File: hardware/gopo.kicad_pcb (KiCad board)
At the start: 4 copper layers, 65.9 x 40.6 mm, 139 parts, among them J3 TFT032B018, J4 SolderWire-1.5sqmm, J7 USB_C_Receptacle_USB2.0_16P, J8 2-CH UART TO ETH, Q1 BSS138P, Q2 BSS138P, Q3 SQJB60EP, Q4 BSS138P, Q5 SQJB60EP, Q6 BSS138P, Q7 IRLML6344, Q8 TSM3443CX6, SW1 BOOT / PTS810, SW2 RESET / PTS810, SW3 L-KLS4-EC1121S-E5A-F12.5, U1 AP33772SDKZ-13-FA02, U10 USBLC6-2SC6, U11 TPS55340PWPR, U12 LM74801-Q1, U13 74LVC1G08, U2 ESP32-C6-MINI-1-H4, U3 INA226, U4 BQ32000, U5 AOZ1284PI, U6 TLV431BQDBZT, Y1 32.768kHz

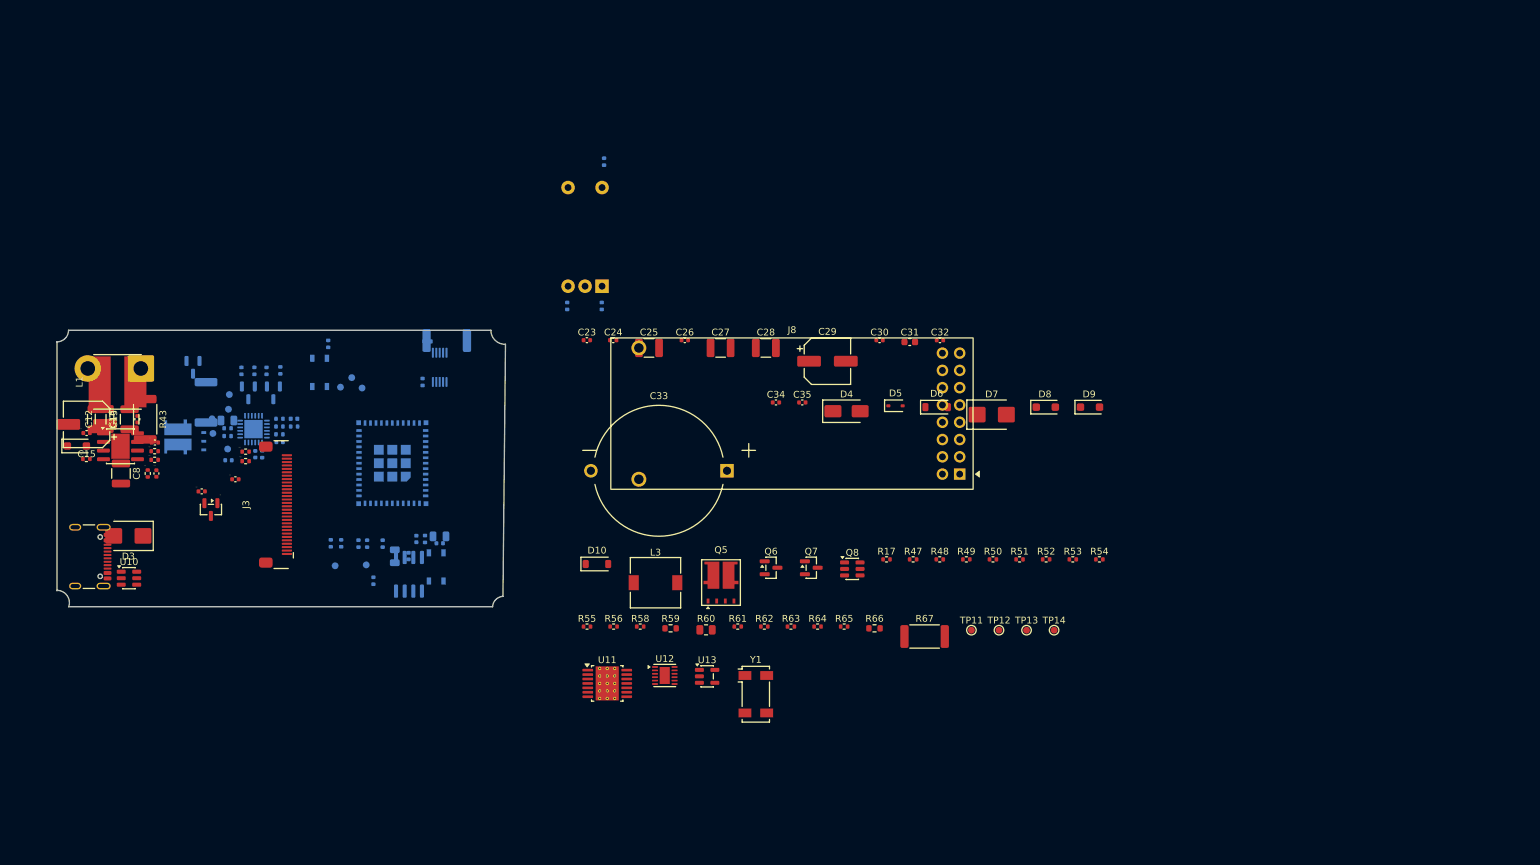
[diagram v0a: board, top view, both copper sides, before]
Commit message: hardware: kart dis hattini TFT032B018 gorunur alanina gore ciz (TASK-062)
107 x 61 mm, r 3; orijin AA merkezi; LCD/AA referansi Dwgs.User'da;
4 x M3 NPTH; U2 anteni sag kenarda, LCD'den 15.2 mm. TFT032B018
mekanik cizimi eklendi. Karar: KART_DIS_HATTI_LCD_20260924.md.

Co-Authored-By: Claude Opus 5.5 <noreply@anthropic.com>
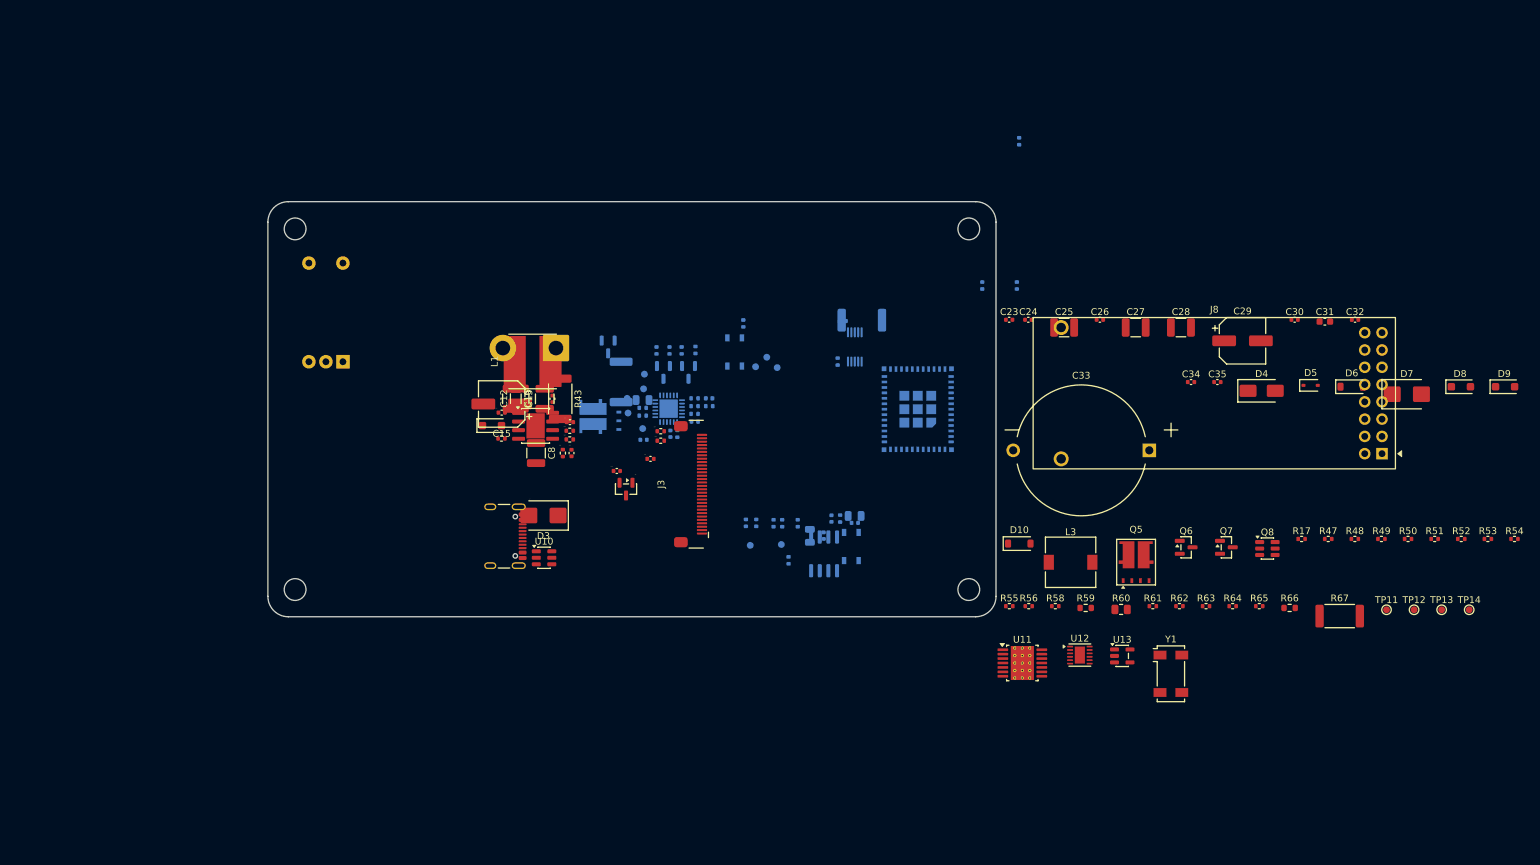
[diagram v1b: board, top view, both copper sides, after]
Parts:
- added H1: M3, MountingHole:MountingHole_3.2mm_M3, F.Cu at (59.5, 73.5)
- added H2: M3, MountingHole:MountingHole_3.2mm_M3, F.Cu at (158.5, 73.5)
- added H3: M3, MountingHole:MountingHole_3.2mm_M3, F.Cu at (59.5, 126.5)
- added H4: M3, MountingHole:MountingHole_3.2mm_M3, F.Cu at (158.5, 126.5)
- moved U2 77.6 mm to (151.0, 100.0)
- moved C23 62.1 mm to (164.4, 86.9)
- moved C33 62.1 mm to (185.0, 106.0)
- moved J8 62.1 mm to (219.2, 106.5)
- moved R55 62.1 mm to (164.5, 128.9)
- moved D10 62.1 mm to (165.9, 119.7)
- moved C11 61.1 mm to (140.0, 87.0)
- moved C26 61.1 mm to (177.8, 86.9)
- moved C6 61.1 mm to (141.7, 116.7)
- moved C7 61.1 mm to (138.3, 116.1)
- moved C9 61.1 mm to (137.2, 118.6)
- moved R15 61.1 mm to (131.1, 116.8)
- moved R16 61.1 mm to (133.4, 116.8)
- moved R60 61.1 mm to (180.9, 129.4)
- moved R61 61.1 mm to (185.5, 128.9)
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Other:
- board size 65.9 x 40.6 mm -> 107 x 61 mm
- board text added: "FPC cikisi, arkaya bukum"
- board text added: "LCD modul 77.70 x 55.04 / pencere AA+0.4"
- board text added: "LCD+15 mm"
- board text added: "TFT032B018 AA 64.80 x 48.60 - orijin AA merkezi"

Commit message: hardware: kart dis hattini AA'ya gore simetrik yap (TASK-062)
99.40 x 61.04 mm: sag/sol kenar AA'dan esit 17.30 mm, ust/alt LCD
modulunden 3 mm. U2 anten varsayimi kaldirildi (konum TASK-063/054).
M3 delikleri +-45.70/+-26.52.

Co-Authored-By: Claude Opus 5.5 <noreply@anthropic.com>
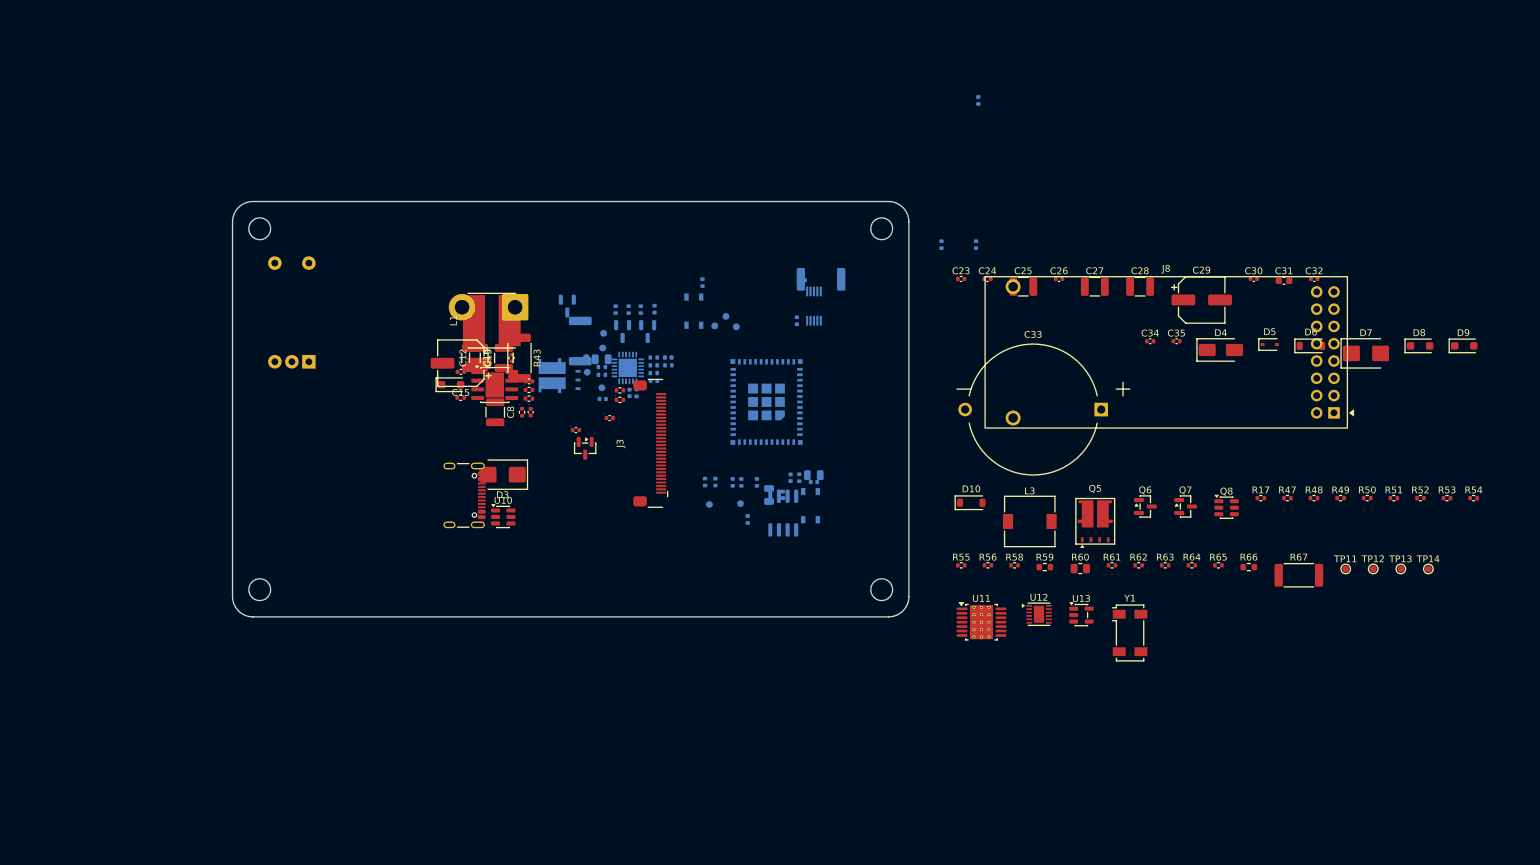
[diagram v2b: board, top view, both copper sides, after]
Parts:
- moved U2 22.2 mm to (128.8, 98.9)
- moved H2 12.8 mm to (145.7, 73.5)
- moved H4 12.8 mm to (145.7, 126.5)
- moved R55 9.26 mm to (157.4, 122.9)
- moved C23 9.26 mm to (157.4, 80.9)
- moved C33 9.26 mm to (178.0, 100.0)
- moved J8 9.26 mm to (212.2, 100.5)
- moved D10 9.26 mm to (158.9, 113.7)
- moved R15 8.49 mm to (125.1, 110.8)
- moved R16 8.49 mm to (127.4, 110.8)
- moved R56 8.49 mm to (161.3, 122.9)
- moved R58 8.49 mm to (165.2, 122.9)
- moved R61 8.49 mm to (179.5, 122.9)
- moved R62 8.49 mm to (183.5, 122.9)
- moved R63 8.49 mm to (187.4, 122.9)
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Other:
- board size 107 x 61 mm -> 99.4 x 61 mm
- board text removed: "LCD+15 mm"

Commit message: hardware: baslangic yerlesimi, bloklar kart disinda gruplu; J3 kilitli (TASK-067)
Co-Authored-By: Claude Opus 5.5 <noreply@anthropic.com>
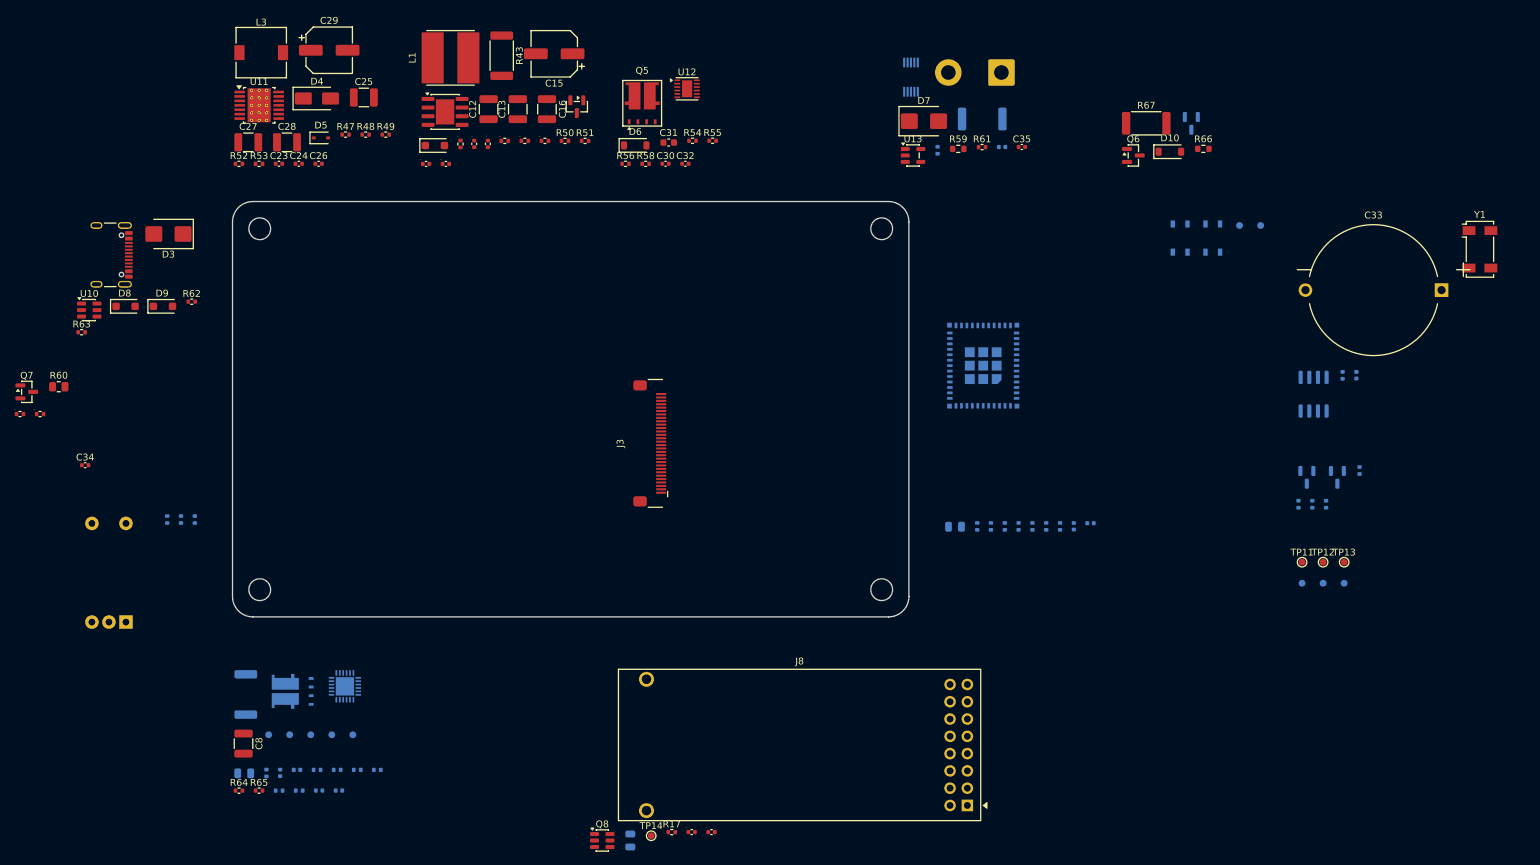
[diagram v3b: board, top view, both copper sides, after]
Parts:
- moved D9 191.3 mm to (40.1, 84.9)
- moved D8 190.3 mm to (34.6, 84.9)
- moved R53 181.4 mm to (54.2, 63.9)
- moved R52 180.4 mm to (51.2, 63.9)
- moved Q7 171.1 mm to (20.1, 97.5)
- moved R63 162.9 mm to (28.1, 88.7)
- moved C34 157.6 mm to (28.6, 108.2)
- moved R60 152.5 mm to (24.8, 96.7)
- moved R49 150.1 mm to (72.8, 59.6)
- moved R48 149.2 mm to (69.9, 59.6)
- moved R47 148.4 mm to (66.9, 59.6)
- moved R65 144.8 mm to (54.2, 156.0)
- moved R62 144.4 mm to (44.3, 84.2)
- moved R64 143.9 mm to (51.2, 156.0)
- moved D5 142.7 mm to (63.3, 60.1)
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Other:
- board text added: "AOZ1284 3.3V BUCK"
- board text added: "AP33772S PD KONTROLCU + VBUS SONT / ANAHTAR"
- board text added: "CIKIS DESARJI (R59 yerine aktif)"
- board text added: "ESP32-C6-MINI-1-H4"
- board text added: "ETHERNET MEZANIN (CH9121) + BESLEME ANAHTARI"
- board text added: "I2C SEVIYE DONUSTURUCU 5V <-> 3.3V"
- board text added: "INA226 OLCUM + PANEL CIKISI"
- board text added: "LM74801 CIKIS ANAHTARI + IDEAL DIYOT"
- board text added: "ROTARY ENCODER"
- board text added: "RTC BQ32000 + 1F5 süper kapasitör"
- board text added: "TEST NOKTALARI"
- board text added: "TFT BACKLIGHT (3.3V + PWM)"
- board text added: "TFT CONNECTOR J3"
- board text added: "TPS55340 PRE-BOOST"
- board text added: "USB-C GIRIS"
